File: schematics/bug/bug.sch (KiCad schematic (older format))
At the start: 15 parts, among them P1 CONN_01X09, P3 CONN_01X06, P4 CONN_01X02, U1 uln2803A, U2 Arduino_Mini, U3 SPX2920U-3.3, U4 ESP8266, U5 button

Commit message: Update schematic
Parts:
- removed U5: button, bugs:button, symbol button
- added P2: CONN_01X04, Pin_Headers:Pin_Header_Straight_1x04, symbol CONN_01X04
- added P5, P6: CONN_01X01, Socket_Strips:Socket_Strip_Straight_1x01, symbol CONN_01X01
- added P7: CONN_01X02, Pin_Headers:Pin_Header_Straight_1x02, symbol CONN_01X02
- added R5: R, Resistors_ThroughHole:Resistor_Horizontal_RM7mm, symbol R
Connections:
- net at P1.9 (P9), U1.10 (COM), U2.7 (RAW)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: now also P7.1 (P1)
- net at U2.10 (VCC): now also P5.1 (P1)
- net at U2.15 (13): now also P2.1 (P1)
- net at U2.16 (12): now also P2.2 (P2)
- net at U2.17 (11): now also P2.3 (P3)
- net at U2.18 (10): now also P2.4 (P4)
- net at C1.2, D1.1 (K), D2.1 (K)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: now also R5.1
- net at P4.1 (P1): now also P7.2 (P2)
- new net: P6.1 (P1), R5.2
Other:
- moved on the sheet: P4
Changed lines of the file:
@@
 L CONN_01X02 P4
 U 1 1 56F1CB48
-P 4800 1600
-F 0 "P4" H 4800 1750 50  0000 C CNN
-F 1 "CONN_01X02" V 4900 1600 50  0000 C CNN
-F 2 "Pin_Headers:Pin_Header_Straight_1x02" H 4800 1600 50  0001 C CNN
-F 3 "" H 4800 1600 50  0000 C CNN
-	1    4800 1600
+P 4800 1000
+F 0 "P4" H 4800 1150 50  0000 C CNN
+F 1 "CONN_01X02" V 4900 1000 50  0000 C CNN
+F 2 "Pin_Headers:Pin_Header_Straight_1x02" H 4800 1000 50  0001 C CNN
+F 3 "" H 4800 1000 50  0000 C CNN
+	1    4800 1000
 	-1   0    0    1
 $EndComp
@@
 	1    0    0    -1
 $EndComp
-$Comp
-L button U5
-U 1 1 56F2F512
-P 5350 1150
-F 0 "U5" H 5400 1150 60  0000 C CNN
-F 1 "button" H 5400 1150 60  0000 C CNN
-F 2 "bugs:button" H 5400 1150 60  0001 C CNN
-F 3 "" H 5400 1150 60  0000 C CNN
-	1    5350 1150
-	1    0    0    -1
-$EndComp
 Wire Wire Line
 	7250 3650 7100 3650
@@
 	6400 2550 6400 2750
 Wire Wire Line
-	5750 1550 5750 2550
+	5750 2550 5750 950
 Connection ~ 5650 2400
 Wire Wire Line
@@
 	4300 3450 4150 3450
 Wire Wire Line
-	7250 5750 6800 5750
+	6800 5750 7250 5750
 Wire Wire Line
 	6900 3500 6900 3650
@@
 Connection ~ 7100 5750
 Wire Wire Line
-	7250 4850 7250 5750
+	7250 5750 7250 4850
 Wire Wire Line
 	7100 4850 7350 4850
@@
 Connection ~ 7250 4850
 Wire Wire Line
-	3200 2050 3200 3350
+	3200 2000 3200 3350
 Connection ~ 3200 3350
 Wire Wire Line
@@
 	6300 4850 6800 4850
 Wire Wire Line
-	5000 1550 5750 1550
-Wire Wire Line
-	5000 1650 5350 1650
-Wire Wire Line
-	4200 2550 6400 2550
+	5750 950  5000 950
+Wire Wire Line
+	5000 1050 5000 1300
+Wire Wire Line
+	2500 2550 6400 2550
 Wire Wire Line
 	4200 3350 4200 2550
@@
 Connection ~ 4200 3350
 Wire Wire Line
-	5350 1650 5350 1450
-Wire Wire Line
-	3200 2050 5250 2050
-Wire Wire Line
-	5250 2050 5250 1450
-Wire Wire Line
-	5100 800  5650 800
-Wire Wire Line
-	5650 800  5650 2400
-Wire Wire Line
-	5250 800  5250 850
-Wire Wire Line
-	5250 1500 5100 1500
-Wire Wire Line
-	5100 1500 5100 800
-Connection ~ 5250 800
-Connection ~ 5250 1500
-Wire Wire Line
 	5400 3450 5550 3450
 Wire Wire Line
@@
 Wire Wire Line
 	5550 3350 5550 4800
+$Comp
+L CONN_01X04 P2
+U 1 1 57121D04
+P 5900 4000
+F 0 "P2" H 5900 4250 50  0000 C CNN
+F 1 "CONN_01X04" V 6000 4000 50  0000 C CNN
+F 2 "Pin_Headers:Pin_Header_Straight_1x04" H 5900 4000 50  0001 C CNN
+F 3 "" H 5900 4000 50  0000 C CNN
+	1    5900 4000
+	1    0    0    -1
+$EndComp
+Wire Wire Line
+	5700 3850 5400 3850
+Wire Wire Line
+	5400 3950 5700 3950
+Wire Wire Line
+	5700 4050 5400 4050
+Wire Wire Line
+	5400 4150 5700 4150
+Wire Wire Line
+	5400 3350 5450 3350
+Wire Wire Line
+	5450 3350 5450 1750
+Wire Wire Line
+	5450 1750 2100 1750
+Connection ~ 4200 2550
+$Comp
+L R R5
+U 1 1 57122C38
+P 2350 2550
+F 0 "R5" V 2430 2550 50  0000 C CNN
+F 1 "R" V 2350 2550 50  0000 C CNN
+F 2 "Resistors_ThroughHole:Resistor_Horizontal_RM7mm" V 2280 2550 50  0001 C CNN
+F 3 "" H 2350 2550 50  0000 C CNN
+	1    2350 2550
+	0    1    1    0
+$EndComp
+$Comp
+L CONN_01X01 P6
+U 1 1 57122CBD
+P 1900 2550
+F 0 "P6" H 1900 2650 50  0000 C CNN
+F 1 "CONN_01X01" V 2000 2550 50  0000 C CNN
+F 2 "Socket_Strips:Socket_Strip_Straight_1x01" H 1900 2550 50  0001 C CNN
+F 3 "" H 1900 2550 50  0000 C CNN
+	1    1900 2550
+	-1   0    0    1
+$EndComp
+$Comp
+L CONN_01X01 P5
+U 1 1 57122DD6
+P 1900 1750
+F 0 "P5" H 1900 1850 50  0000 C CNN
+F 1 "CONN_01X01" V 2000 1750 50  0000 C CNN
+F 2 "Socket_Strips:Socket_Strip_Straight_1x01" H 1900 1750 50  0001 C CNN
+F 3 "" H 1900 1750 50  0000 C CNN
+	1    1900 1750
+	-1   0    0    1
+$EndComp
+Wire Wire Line
+	2200 2550 2100 2550
+$Comp
+L CONN_01X02 P7
+U 1 1 5712384B
+P 4800 1350
+F 0 "P7" H 4800 1500 50  0000 C CNN
+F 1 "CONN_01X02" V 4900 1350 50  0000 C CNN
+F 2 "Pin_Headers:Pin_Header_Straight_1x02" H 4800 1350 50  0001 C CNN
+F 3 "" H 4800 1350 50  0000 C CNN
+	1    4800 1350
+	-1   0    0    1
+$EndComp
+Wire Wire Line
+	5000 1400 5000 2000
+Wire Wire Line
+	3200 2000 5650 2000
+Wire Wire Line
+	5650 2000 5650 2400
+Connection ~ 5000 2000
 $EndSCHEMATC

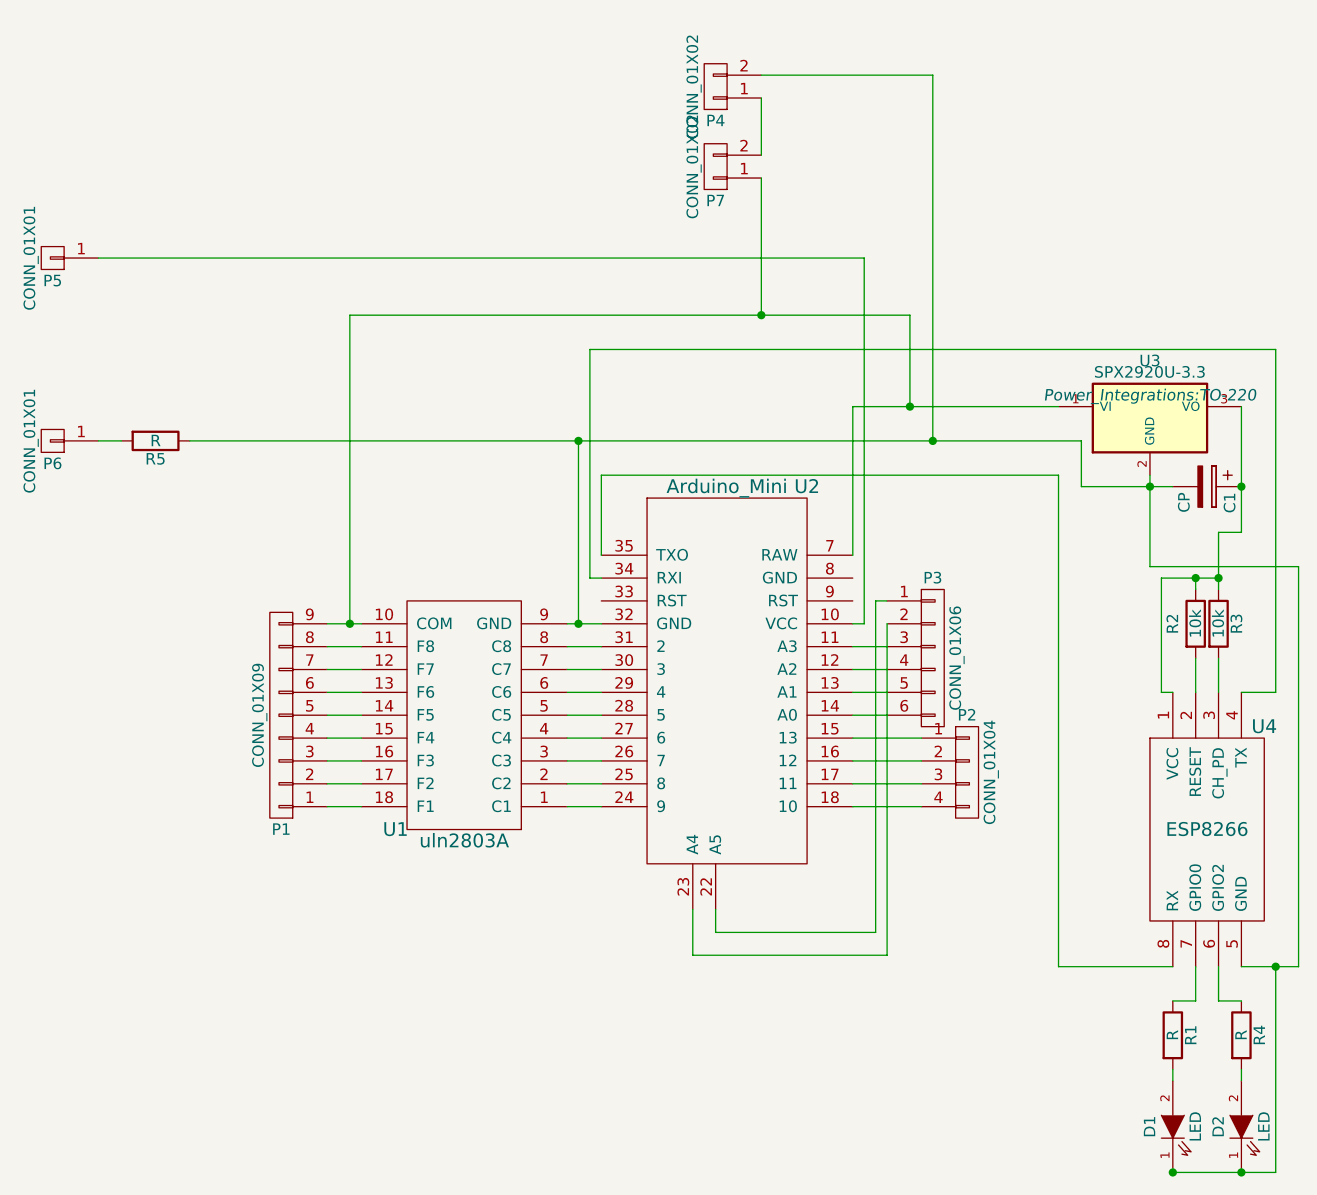
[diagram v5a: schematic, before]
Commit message: Update schematics for whiskers
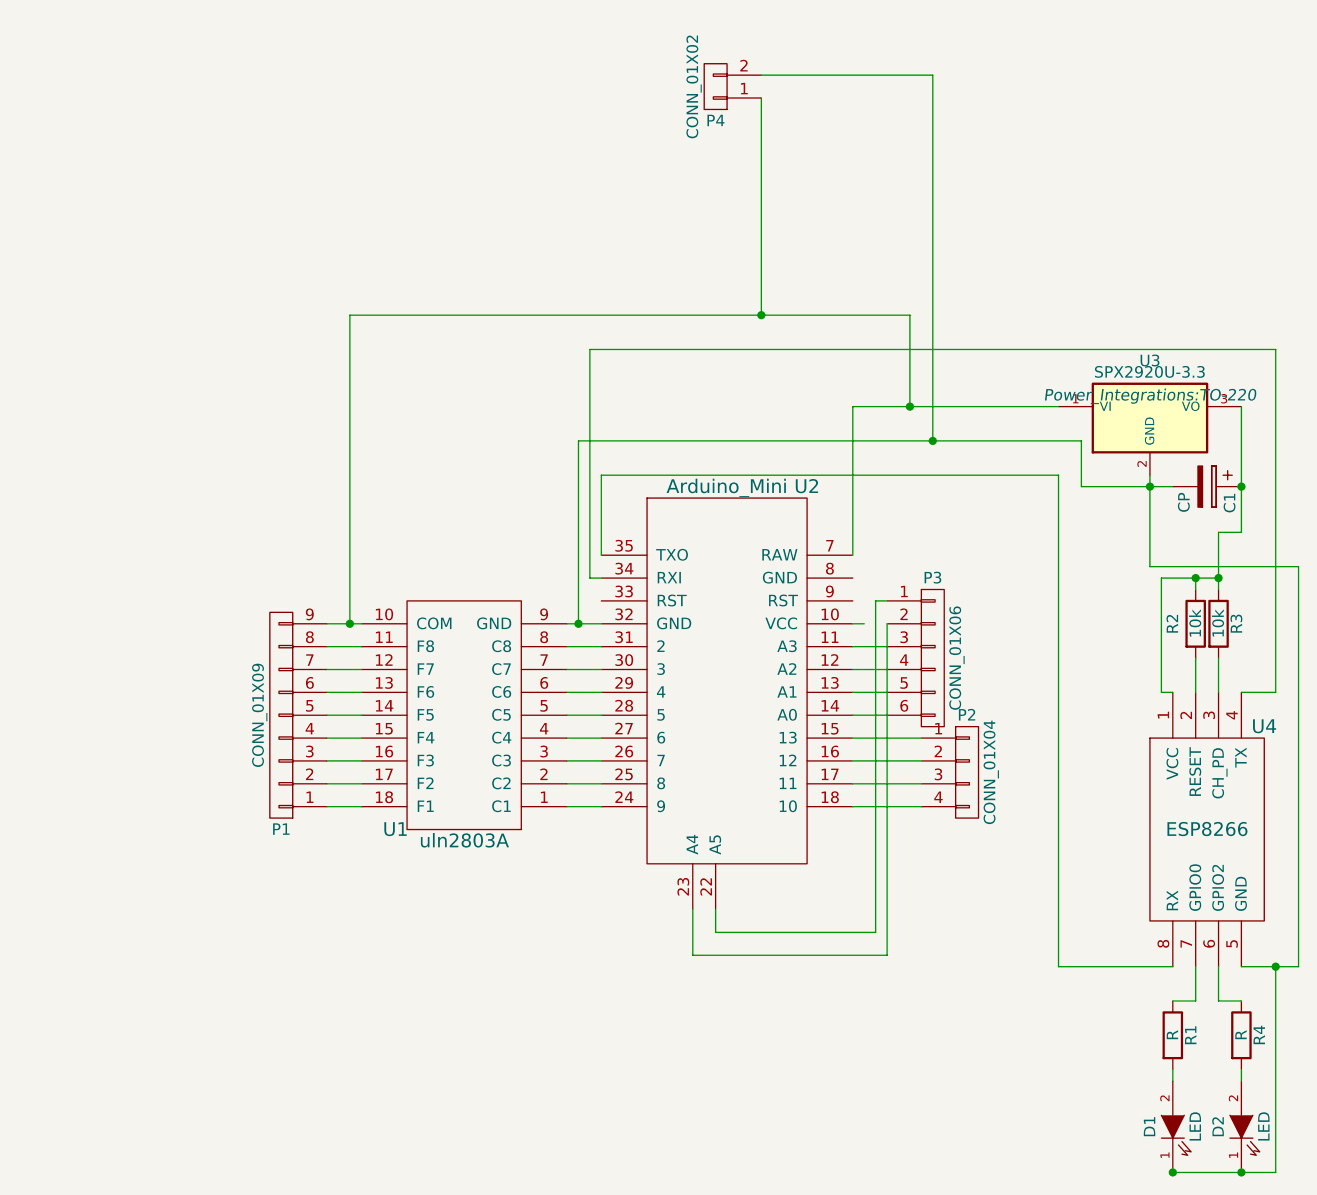
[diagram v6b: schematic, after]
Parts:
- removed P5, P6: CONN_01X01, Socket_Strips:Socket_Strip_Straight_1x01, symbol CONN_01X01
- removed P7: CONN_01X02, Pin_Headers:Pin_Header_Straight_1x02, symbol CONN_01X02
- removed R5: R, Resistors_ThroughHole:Resistor_Horizontal_RM7mm, symbol R
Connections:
- net at P1.9 (P9), U1.10 (COM), U2.7 (RAW)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: now also P4.1 (P1)
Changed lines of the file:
@@
 	5750 950  5000 950
 Wire Wire Line
-	5000 1050 5000 1300
-Wire Wire Line
-	2500 2550 6400 2550
+	5000 1050 5000 2000
 Wire Wire Line
 	4200 3350 4200 2550
@@
 	5400 3350 5450 3350
 Wire Wire Line
-	5450 3350 5450 1750
-Wire Wire Line
-	5450 1750 2100 1750
-Connection ~ 4200 2550
-$Comp
-L R R5
-U 1 1 57122C38
-P 2350 2550
-F 0 "R5" V 2430 2550 50  0000 C CNN
-F 1 "R" V 2350 2550 50  0000 C CNN
-F 2 "Resistors_ThroughHole:Resistor_Horizontal_RM7mm" V 2280 2550 50  0001 C CNN
-F 3 "" H 2350 2550 50  0000 C CNN
-	1    2350 2550
-	0    1    1    0
-$EndComp
-$Comp
-L CONN_01X01 P6
-U 1 1 57122CBD
-P 1900 2550
-F 0 "P6" H 1900 2650 50  0000 C CNN
-F 1 "CONN_01X01" V 2000 2550 50  0000 C CNN
-F 2 "Socket_Strips:Socket_Strip_Straight_1x01" H 1900 2550 50  0001 C CNN
-F 3 "" H 1900 2550 50  0000 C CNN
-	1    1900 2550
-	-1   0    0    1
-$EndComp
-$Comp
-L CONN_01X01 P5
-U 1 1 57122DD6
-P 1900 1750
-F 0 "P5" H 1900 1850 50  0000 C CNN
-F 1 "CONN_01X01" V 2000 1750 50  0000 C CNN
-F 2 "Socket_Strips:Socket_Strip_Straight_1x01" H 1900 1750 50  0001 C CNN
-F 3 "" H 1900 1750 50  0000 C CNN
-	1    1900 1750
-	-1   0    0    1
-$EndComp
-Wire Wire Line
-	2200 2550 2100 2550
-$Comp
-L CONN_01X02 P7
-U 1 1 5712384B
-P 4800 1350
-F 0 "P7" H 4800 1500 50  0000 C CNN
-F 1 "CONN_01X02" V 4900 1350 50  0000 C CNN
-F 2 "Pin_Headers:Pin_Header_Straight_1x02" H 4800 1350 50  0001 C CNN
-F 3 "" H 4800 1350 50  0000 C CNN
-	1    4800 1350
-	-1   0    0    1
-$EndComp
-Wire Wire Line
-	5000 1400 5000 2000
-Wire Wire Line
 	3200 2000 5650 2000
 Wire Wire Line
 	5650 2000 5650 2400
 Connection ~ 5000 2000
+Wire Wire Line
+	4200 2550 6400 2550
 $EndSCHEMATC

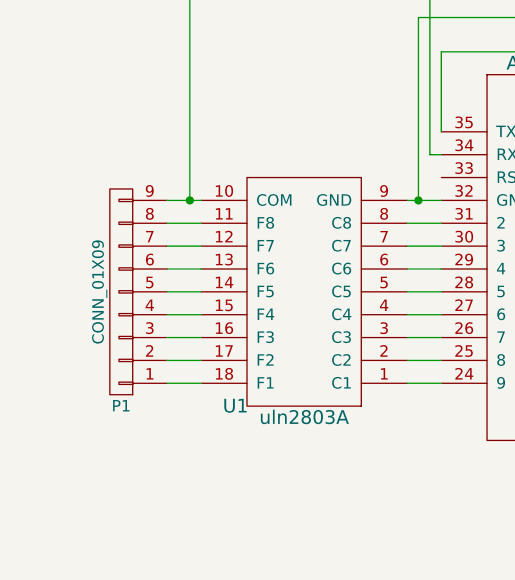
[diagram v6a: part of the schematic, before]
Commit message: Update bug schematic
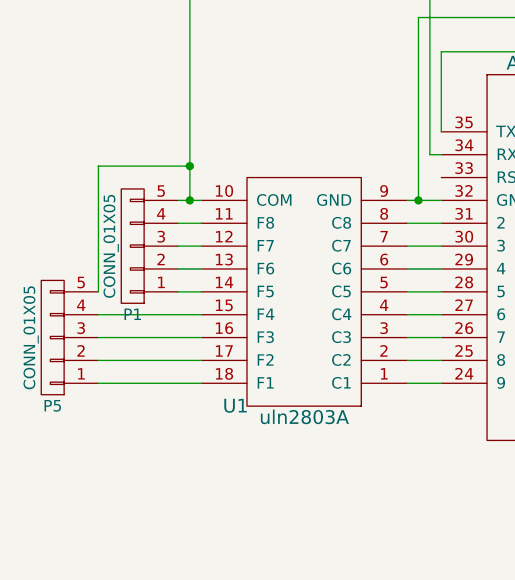
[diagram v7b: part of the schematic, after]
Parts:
- removed P1: CONN_01X09, Pin_Headers:Pin_Header_Straight_1x09, symbol CONN_01X09
- added P1, P5: CONN_01X05, Pin_Headers:Pin_Header_Straight_1x05, symbol CONN_01X05
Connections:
- net at U1.18 (F1): now also P5.1 (P1)
- net at U1.17 (F2): now also P5.2 (P2)
- net at U1.16 (F3): now also P5.3 (P3)
- net at U1.15 (F4): now also P5.4 (P4)
- net at U1.14 (F5): now also P1.1 (P1)
- net at U1.13 (F6): now also P1.2 (P2)
- net at U1.12 (F7): now also P1.3 (P3)
- net at U1.11 (F8): now also P1.4 (P4)
- net at P4.1 (P1), U1.10 (COM), U2.7 (RAW)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: now also P1.5 (P5), P5.5 (P5)
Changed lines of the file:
@@
 $EndDescr
-$Comp
-L CONN_01X09 P1
-U 1 1 56F1A493
-P 2900 3750
-F 0 "P1" H 2900 4250 50  0000 C CNN
-F 1 "CONN_01X09" V 3000 3750 50  0000 C CNN
-F 2 "Pin_Headers:Pin_Header_Straight_1x09" H 2900 3750 50  0001 C CNN
-F 3 "" H 2900 3750 50  0000 C CNN
-	1    2900 3750
-	-1   0    0    1
-$EndComp
 $Comp
 L uln2803A U1
@@
 	1    0    0    -1
 $EndComp
-Wire Wire Line
-	7250 3650 7100 3650
-Wire Wire Line
-	4300 3850 4150 3850
-Wire Wire Line
-	4150 3950 4300 3950
-Wire Wire Line
-	4300 4150 4150 4150
-Connection ~ 6900 3150
-Wire Wire Line
-	6750 3650 6800 3650
-Wire Wire Line
-	6750 3150 6750 3650
-Connection ~ 7000 3150
-Wire Wire Line
-	6900 3150 6900 3200
-Wire Wire Line
-	6750 3150 7000 3150
-Connection ~ 7100 2750
-Wire Wire Line
-	7000 2950 7000 3200
-Wire Wire Line
-	7100 2950 7000 2950
-Wire Wire Line
-	7100 2400 7100 2950
-Wire Wire Line
-	6400 2750 6800 2750
-Wire Wire Line
-	6700 2700 6700 3100
-Wire Wire Line
-	6400 2550 6400 2750
-Wire Wire Line
-	5750 2550 5750 950
-Connection ~ 5650 2400
-Wire Wire Line
-	5400 2400 5400 3050
-Wire Wire Line
-	5400 2400 6300 2400
-Wire Wire Line
-	4700 4800 4700 4600
-Wire Wire Line
-	4800 4600 4800 4700
-Wire Wire Line
-	3100 3350 3250 3350
-Wire Wire Line
-	3100 3450 3250 3450
-Wire Wire Line
-	3250 3550 3100 3550
-Wire Wire Line
-	3100 3650 3250 3650
-Wire Wire Line
-	3250 3750 3100 3750
-Wire Wire Line
-	3100 3850 3250 3850
-Wire Wire Line
-	3250 3950 3100 3950
-Wire Wire Line
-	3100 4050 3250 4050
-Wire Wire Line
-	3250 4150 3100 4150
-Wire Wire Line
-	4300 4050 4150 4050
-Wire Wire Line
-	4150 3750 4300 3750
-Wire Wire Line
-	4300 3650 4150 3650
-Wire Wire Line
-	4150 3550 4300 3550
-Wire Wire Line
-	4300 3450 4150 3450
-Wire Wire Line
-	6800 5750 7250 5750
-Wire Wire Line
-	6900 3500 6900 3650
-Wire Wire Line
-	7000 3500 7000 3650
-Connection ~ 6800 5750
-Connection ~ 7100 5750
-Wire Wire Line
-	7250 5750 7250 4850
-Wire Wire Line
-	7100 4850 7350 4850
-Wire Wire Line
-	6800 5300 6800 5350
-Wire Wire Line
-	7100 5350 7100 5300
-Wire Wire Line
-	6900 5000 6800 5000
-Wire Wire Line
-	6900 4850 6900 5000
-Wire Wire Line
-	7000 5000 7000 4850
-Wire Wire Line
-	7100 5000 7000 5000
-Wire Wire Line
-	7350 4850 7350 3100
-Wire Wire Line
-	7350 3100 6700 3100
-Connection ~ 6700 2750
-Connection ~ 7250 4850
-Wire Wire Line
-	3200 2000 3200 3350
-Connection ~ 3200 3350
-Wire Wire Line
-	4150 3350 4300 3350
-Wire Wire Line
-	7250 3650 7250 2150
-Wire Wire Line
-	7250 2150 4250 2150
-Wire Wire Line
-	4250 2150 4250 3150
-Wire Wire Line
-	4250 3150 4300 3150
-Wire Wire Line
-	4300 3050 4300 2700
-Wire Wire Line
-	4300 2700 6300 2700
-Wire Wire Line
-	6300 2700 6300 4850
-Wire Wire Line
-	6300 4850 6800 4850
-Wire Wire Line
-	5750 950  5000 950
-Wire Wire Line
-	5000 1050 5000 2000
-Wire Wire Line
-	4200 3350 4200 2550
-Connection ~ 5750 2550
-Connection ~ 4200 3350
-Wire Wire Line
-	5400 3450 5550 3450
-Wire Wire Line
-	5400 3550 5550 3550
-Wire Wire Line
-	5400 3650 5550 3650
-Wire Wire Line
-	5400 3750 5550 3750
-Wire Wire Line
-	5550 4800 4700 4800
-Wire Wire Line
-	4800 4700 5500 4700
-Wire Wire Line
-	5500 4700 5500 3250
-Wire Wire Line
-	5500 3250 5550 3250
-Wire Wire Line
-	5550 3350 5550 4800
 $Comp
 L CONN_01X04 P2
@@
 	1    0    0    -1
 $EndComp
+$Comp
+L CONN_01X05 P1
+U 1 1 572B3424
+P 2950 3550
+F 0 "P1" H 2950 3850 50  0000 C CNN
+F 1 "CONN_01X05" V 3050 3550 50  0000 C CNN
+F 2 "Pin_Headers:Pin_Header_Straight_1x05" H 2950 3550 50  0001 C CNN
+F 3 "" H 2950 3550 50  0000 C CNN
+	1    2950 3550
+	-1   0    0    1
+$EndComp
+$Comp
+L CONN_01X05 P5
+U 1 1 572B3498
+P 2600 3950
+F 0 "P5" H 2600 4250 50  0000 C CNN
+F 1 "CONN_01X05" V 2700 3950 50  0000 C CNN
+F 2 "Pin_Headers:Pin_Header_Straight_1x05" H 2600 3950 50  0001 C CNN
+F 3 "" H 2600 3950 50  0000 C CNN
+	1    2600 3950
+	-1   0    0    1
+$EndComp
+Wire Wire Line
+	7250 3650 7100 3650
+Wire Wire Line
+	4300 3850 4150 3850
+Wire Wire Line
+	4150 3950 4300 3950
+Wire Wire Line
+	4300 4150 4150 4150
+Connection ~ 6900 3150
+Wire Wire Line
+	6750 3650 6800 3650
+Wire Wire Line
+	6750 3150 6750 3650
+Connection ~ 7000 3150
+Wire Wire Line
+	6900 3150 6900 3200
+Wire Wire Line
+	6750 3150 7000 3150
+Connection ~ 7100 2750
+Wire Wire Line
+	7000 2950 7000 3200
+Wire Wire Line
+	7100 2950 7000 2950
+Wire Wire Line
+	7100 2400 7100 2950
+Wire Wire Line
+	6400 2750 6800 2750
+Wire Wire Line
+	6700 2700 6700 3100
+Wire Wire Line
+	6400 2550 6400 2750
+Wire Wire Line
+	5750 2550 5750 950
+Connection ~ 5650 2400
+Wire Wire Line
+	5400 2400 5400 3050
+Wire Wire Line
+	5400 2400 6300 2400
+Wire Wire Line
+	4700 4800 4700 4600
+Wire Wire Line
+	4800 4600 4800 4700
+Wire Wire Line
+	3150 3350 3250 3350
+Wire Wire Line
+	3150 3450 3250 3450
+Wire Wire Line
+	3150 3550 3250 3550
+Wire Wire Line
+	3150 3650 3250 3650
+Wire Wire Line
+	3150 3750 3250 3750
+Wire Wire Line
+	2800 3850 3250 3850
+Wire Wire Line
+	2800 3950 3250 3950
+Wire Wire Line
+	2800 4050 3250 4050
+Wire Wire Line
+	2800 4150 3250 4150
+Wire Wire Line
+	4300 4050 4150 4050
+Wire Wire Line
+	4150 3750 4300 3750
+Wire Wire Line
+	4300 3650 4150 3650
+Wire Wire Line
+	4150 3550 4300 3550
+Wire Wire Line
+	4300 3450 4150 3450
+Wire Wire Line
+	6800 5750 7250 5750
+Wire Wire Line
+	6900 3500 6900 3650
+Wire Wire Line
+	7000 3500 7000 3650
+Connection ~ 6800 5750
+Connection ~ 7100 5750
+Wire Wire Line
+	7250 5750 7250 4850
+Wire Wire Line
+	7100 4850 7350 4850
+Wire Wire Line
+	6800 5300 6800 5350
+Wire Wire Line
+	7100 5350 7100 5300
+Wire Wire Line
+	6900 5000 6800 5000
+Wire Wire Line
+	6900 4850 6900 5000
+Wire Wire Line
+	7000 5000 7000 4850
+Wire Wire Line
+	7100 5000 7000 5000
+Wire Wire Line
+	7350 4850 7350 3100
+Wire Wire Line
+	7350 3100 6700 3100
+Connection ~ 6700 2750
+Connection ~ 7250 4850
+Wire Wire Line
+	3200 2000 3200 3350
+Connection ~ 3200 3350
+Wire Wire Line
+	4150 3350 4300 3350
+Wire Wire Line
+	7250 3650 7250 2150
+Wire Wire Line
+	7250 2150 4250 2150
+Wire Wire Line
+	4250 2150 4250 3150
+Wire Wire Line
+	4250 3150 4300 3150
+Wire Wire Line
+	4300 3050 4300 2700
+Wire Wire Line
+	4300 2700 6300 2700
+Wire Wire Line
+	6300 2700 6300 4850
+Wire Wire Line
+	6300 4850 6800 4850
+Wire Wire Line
+	5750 950  5000 950
+Wire Wire Line
+	5000 1050 5000 2000
+Wire Wire Line
+	4200 3350 4200 2550
+Connection ~ 5750 2550
+Connection ~ 4200 3350
+Wire Wire Line
+	5400 3450 5550 3450
+Wire Wire Line
+	5400 3550 5550 3550
+Wire Wire Line
+	5400 3650 5550 3650
+Wire Wire Line
+	5400 3750 5550 3750
+Wire Wire Line
+	5550 4800 4700 4800
+Wire Wire Line
+	4800 4700 5500 4700
+Wire Wire Line
+	5500 4700 5500 3250
+Wire Wire Line
+	5500 3250 5550 3250
+Wire Wire Line
+	5550 3350 5550 4800
 Wire Wire Line
 	5700 3850 5400 3850
@@
 Wire Wire Line
 	4200 2550 6400 2550
+Connection ~ 3200 3200
+Wire Wire Line
+	2800 3750 2800 3200
+Wire Wire Line
+	2800 3200 3200 3200
 $EndSCHEMATC
